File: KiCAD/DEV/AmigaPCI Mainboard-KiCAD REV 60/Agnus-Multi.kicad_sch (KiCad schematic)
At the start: 12 parts, among them J203 RAMEN, J206 CLK/VBB, U202 Agnus_MULTI, U229 74CBT16233

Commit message: APCI Rev 6.0 Work
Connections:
- net R_WA renamed _AWEN
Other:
- note added: "J210"
- note removed: "J211"
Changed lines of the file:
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@@
 	(title_block
 		(title "AMIGA PCI")
-		(date "2025-04-24")
+		(date "2025-04-28")
 		(rev "6.0")
 	)
@@
 		)
 	)
-	(text "J211"
+	(text "J210"
 		(exclude_from_sim no)
 		(at 213.36 232.41 90)
@@
 		)
 	)
-	(global_label "R_WA"
+	(global_label "_AWEN"
 		(shape input)
 		(at 43.18 184.15 180)
@@
 		)
 		(property "Intersheetrefs" "${INTERSHEET_REFS}"
-			(at 35.4172 184.15 0)
+			(at 34.2077 184.15 0)
 			(effects
 				(font

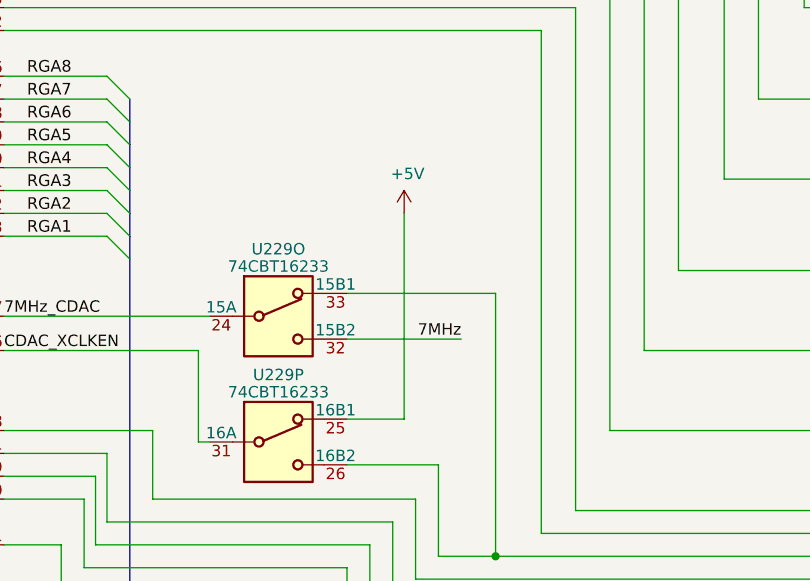
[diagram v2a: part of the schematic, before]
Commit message: APCI Rev 6.0 Work
Eliminate U230 (74LVC147) by moving the clock switching function to U409.
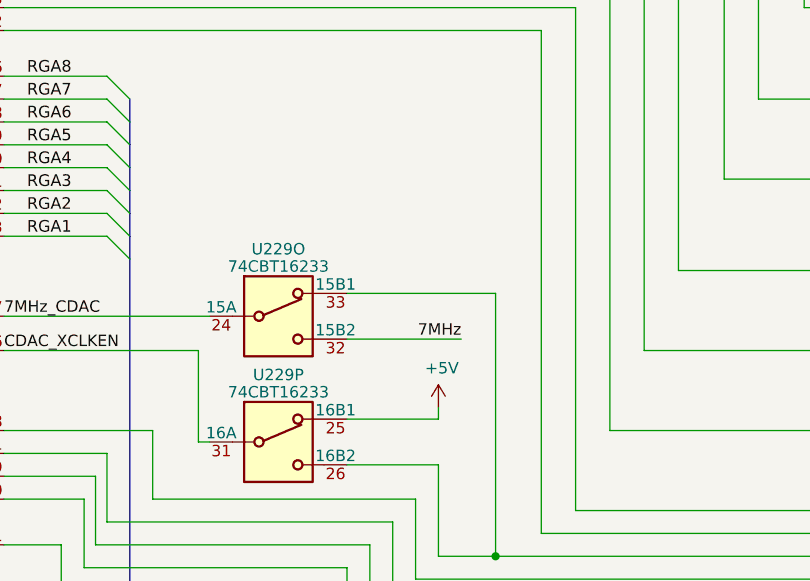
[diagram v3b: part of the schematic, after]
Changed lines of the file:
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@@
 	(wire
 		(pts
-			(xy 293.37 156.21) (xy 293.37 179.07)
+			(xy 297.18 177.8) (xy 297.18 179.07)
 		)
 		(stroke
@@
 	(wire
 		(pts
-			(xy 287.02 179.07) (xy 293.37 179.07)
+			(xy 287.02 179.07) (xy 297.18 179.07)
 		)
 		(stroke
@@
 	(symbol
 		(lib_id "power:+5V")
-		(at 293.37 156.21 0)
+		(at 297.18 177.8 0)
 		(unit 1)
 		(exclude_from_sim no)
@@
 		(dnp no)
 		(property "Reference" "#PWR016"
-			(at 293.37 160.02 0)
+			(at 297.18 181.61 0)
 			(effects
 				(font
@@
 		)
 		(property "Value" "+5V"
-			(at 293.751 151.8158 0)
+			(at 297.561 173.4058 0)
 			(effects
 				(font
@@
 		)
 		(property "Footprint" ""
-			(at 293.37 156.21 0)
+			(at 297.18 177.8 0)
 			(effects
 				(font
@@
 		)
 		(property "Datasheet" ""
-			(at 293.37 156.21 0)
+			(at 297.18 177.8 0)
 			(effects
 				(font
@@
 		)
 		(property "Description" ""
-			(at 293.37 156.21 0)
+			(at 297.18 177.8 0)
 			(effects
 				(font
